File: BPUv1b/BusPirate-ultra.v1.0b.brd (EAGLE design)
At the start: 100 x 50 mm, 176 parts, among them CON1 USB-C-12, IC1 SN74LVC1T45DBV, IC10 23LC1024, IC11 74HCT4051, IC12 MCP1824_ADJ, IC2 SN74LVC1T45DBV, IC3 SN74LVC1T45DBV, IC4 SN74LVC1T45DBV, IC5 SN74LVC1T45DBV, IC6 SN74LVC1T45DBV, IC7 SN74LVC1T45DBV, IC8 SN74LVC1T45DBV, IC9 23LC1024, J1 CON_HEADER_1X04, J2 CON_HEADER_1X10-RIGHT_ANGLED_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, J3 CON_MOLEX_MALE_SMT_SH_1.25, Q1 DMMT3906W, U1 74LVC1G07DBV, U10 74HCT4066PW, U11 74HCT4066PW, U12 W25X40CL, U13 74LVC245A, U14 MCP6001, U15 MCP6001, U16 ICE40HX4K, U2 74LVC1G07DBV, U3 74LVC1G07DBV, U4 74LVC1G07DBV, U5 STM32F103ZX, U6 74LVC1G07DBV, U7 74LVC1G07DBV, U8 74LVC1G07DBV, U9 74LVC1G07DBV

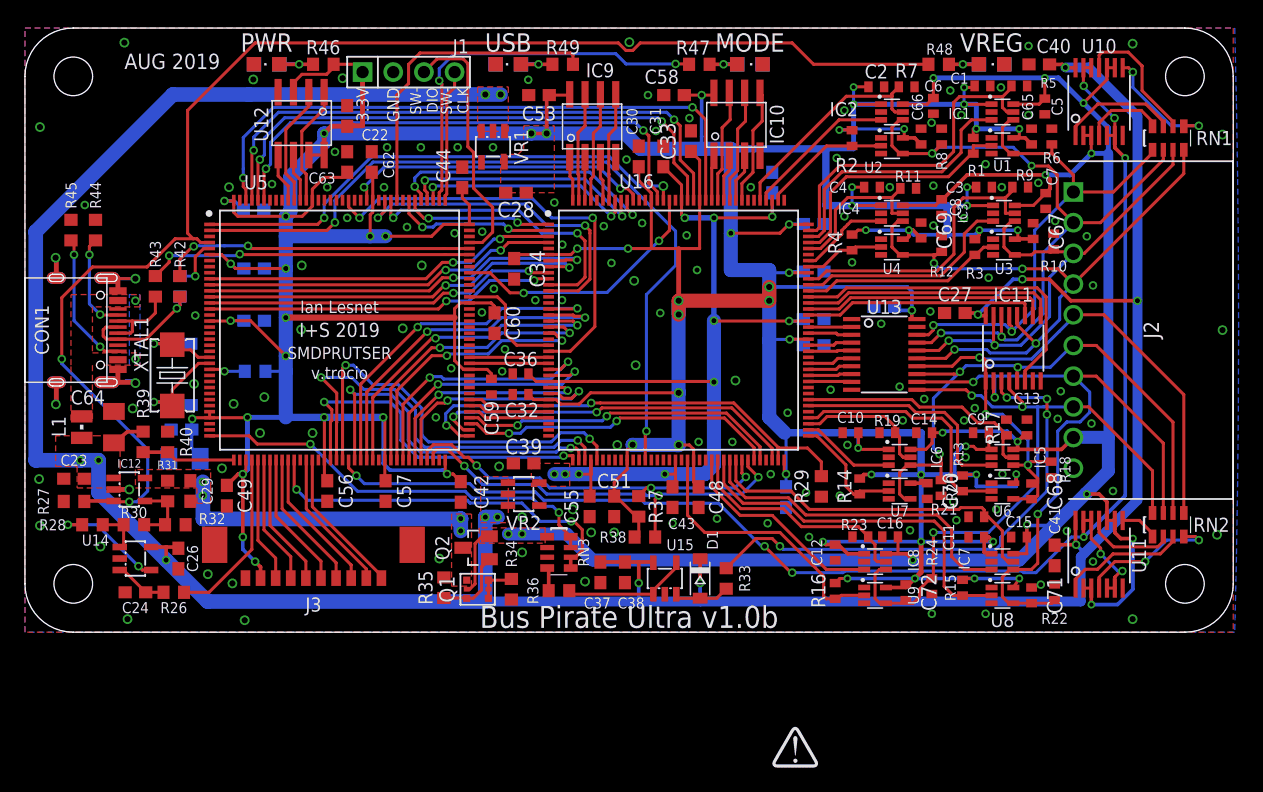
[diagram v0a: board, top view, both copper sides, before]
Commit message: Revert previous commit to v1b, wrong version commited. changes should be on v1c not v1b.
This reverts commit d10a26b079303959180bb4ab2616075854f9b9d1.
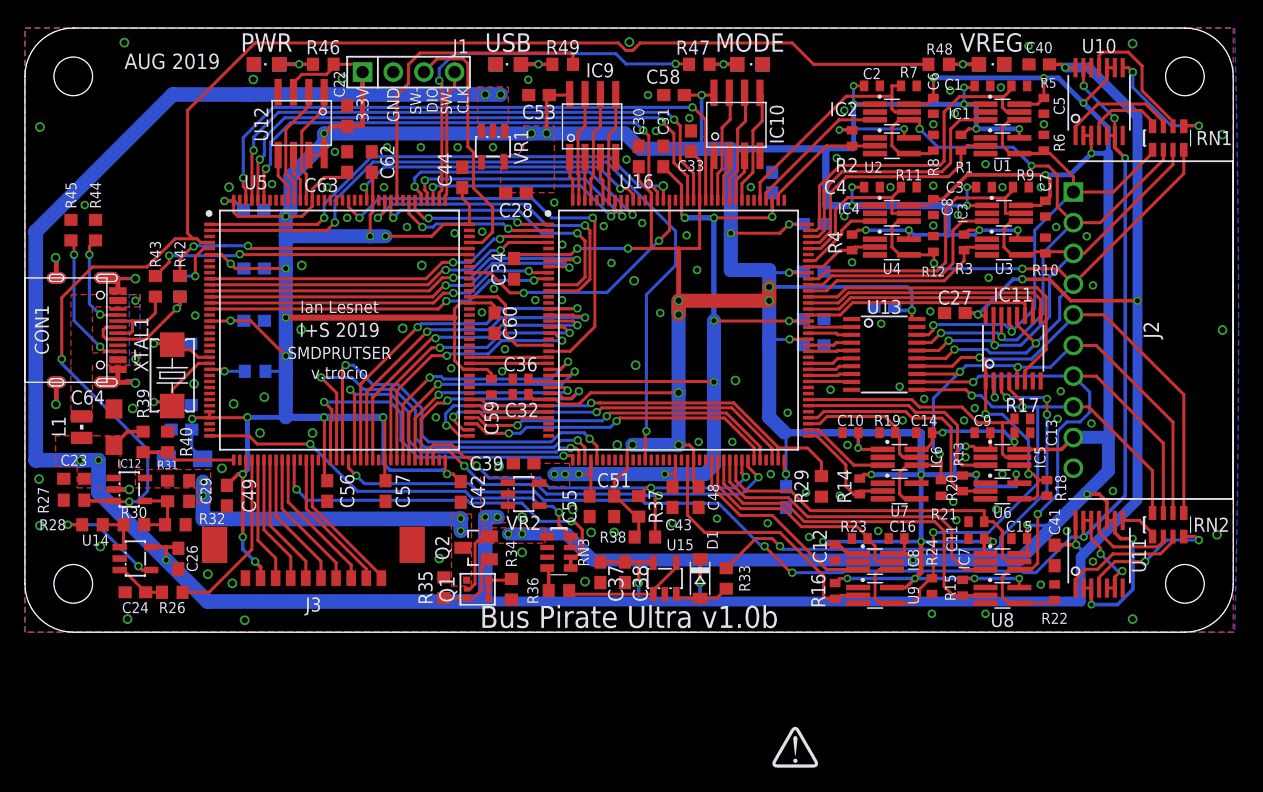
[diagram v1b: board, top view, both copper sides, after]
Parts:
- removed C65, C66, C67, C68, C69, C70, C71, C72: 0.1uF, dp_devices.v6:C402
- C1, C5: device dp_devices.v6:C402 -> rcl:C0402
- C10, C11, C12, C13, C14, C15, C16, C2, C3, C4, C6, C7, C8, C9: device dp_devices.v6:C402 -> resistor:C0402
- C17, C18, C20, C21, C22, C24, C25, C26, C27, C30, C31, C33, C34, C35, C37, C38, C40, C41, C42, C43, C44, C45, C46, C47, C48, C49, C50, C51, C52, C53, C54, C55, C56, C57, C58, C60, C61, C62, C63: device dp_devices.v6:C603 -> rcl:C0603
- C19, C64: device dp_devices.v6:SMC_A -> rcl:SMC_A
- C28, C39: value 1uF -> 1uf; device dp_devices.v6:C603 -> rcl:C0603
- IC1, IC2, IC3, IC4, IC5, IC6, IC7, IC8: device dp_devices.v6:SC-70-6 -> dp_devices.v6:SC-70-6_EXTENDED_PADS
- R1, R10, R11, R12, R13, R14, R15, R16, R17, R18, R19, R2, R20, R21, R22, R23, R24, R3, R4, R5, R6, R7, R8, R9: device dp_devices.v6:R402 -> resistor:R0402
- R26, R29, R37, R38, R41, R42, R43, R44, R45: device dp_devices.v6:R603 -> rcl:R0603
- R33, R36, R39, R40: device dp_devices.v6:R603 -> resistor:R0603
- R46, R47, R48, R49: device dp_devices.v6:R603 -> dp_devices:R603
- U1, U2, U3, U4, U6, U7, U8, U9: device dp_devices.v6:SC-70-5 -> dp_devices.v6:SC-70-5_EXTENDED_PADS
- XTAL1: device dp_devices.v6:XTAL_4X6 -> dp_devices:XTAL_4X6
- moved R18 1.56 mm to (84.6, 11.9)
- moved R17 1.50 mm to (82.5, 17.7), turned to 180 degrees
- moved R1 1.05 mm to (77.5, 40.5)
- moved R3 0.97 mm to (77.7, 32.3)
- moved R8 0.85 mm to (75.2, 40.5)
- moved R6 0.83 mm to (84.3, 40.5)
- moved R10 0.76 mm to (84.5, 32.0)
- moved C8 0.69 mm to (75.2, 35.2), turned to 90 degrees
- moved R12 0.69 mm to (75.2, 32.1)
- moved C7 0.64 mm to (84.5, 35.1), turned to 90 degrees
- moved C13 0.58 mm to (82.5, 16.5), turned to 180 degrees
- moved C16 0.55 mm to (72.1, 7.75), turned to 0 degrees
- moved C36 0.43 mm to (41.0, 21.0)
- moved R21 0.41 mm to (78.7, 9.14)
- moved C2 0.36 mm to (70.1, 45.2), turned to 0 degrees
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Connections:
- net 1V2: now also C31.2, C35.2, C39.1, C43.2, C54.2, C55.2; no longer C31.1, C35.1, C39.2, C43.1, C54.1, C55.1
- net 3V3: now also C1.1, C10.1, C11.1, C12.1, C17.2, C2.1, C21.2, C22.2, C25.2, C28.1, C3.1, C30.2, C33.2, C34.2, C4.1, C42.2, C44.2, C45.2, C46.2, C47.2, C48.2, C49.2, C50.2, C51.2, C52.2, C53.1, C56.2, C57.2, C58.1, C60.2, C61.1, C62.2, C63.2, C9.1; no longer C1.2, C10.2, C11.2, C12.2, C17.1, C2.2, C21.1, C22.1, C25.1, C28.2, C3.2, C30.1, C33.1, C34.1, C4.2, C42.1, C44.1, C45.1, C46.1, C47.1, C48.1, C49.1, C50.1, C51.1, C52.1, C53.2, C56.1, C57.1, C58.2, C60.1, C61.2, C62.1, C63.1, C65.2, C66.2, C67.2, C68.2, C69.2, C70.2, C71.2, C72.2, C9.2
- net GND: now also C1.2, C10.2, C11.2, C12.2, C13.1, C14.1, C15.1, C16.1, C17.1, C18.1, C2.2, C20.1, C21.1, C22.1, C24.2, C25.1, C26.2, C27.2, C28.2, C3.2, C30.1, C31.1, C33.1, C34.1, C35.1, C39.2, C4.2, C40.2, C41.2, C42.1, C43.1, C44.1, C45.1, C46.1, C47.1, C48.1, C49.1, C5.1, C50.1, C51.1, C52.1, C53.2, C54.1, C55.1, C56.1, C57.1, C58.2, C6.1, C60.1, C61.2, C62.1, C63.1, C7.1, C8.1, C9.2; no longer C1.1, C10.1, C11.1, C12.1, C13.2, C14.2, C15.2, C16.2, C17.2, C18.2, C2.1, C20.2, C21.2, C22.2, C24.1, C25.2, C26.1, C27.1, C28.1, C3.1, C30.2, C31.2, C33.2, C34.2, C35.2, C39.1, C4.1, C40.1, C41.1, C42.2, C43.2, C44.2, C45.2, C46.2, C47.2, C48.2, C49.2, C5.2, C50.2, C51.2, C52.2, C53.1, C54.2, C55.2, C56.2, C57.2, C58.1, C6.2, C60.2, C61.1, C62.2, C63.2, C65.1, C66.1, C67.1, C68.1, C69.1, C7.2, C70.1, C71.1, C72.1, C8.2, C9.1
- net N$31: now also C24.1; no longer C24.2
- net N$8: now also C20.2; no longer C20.1
- net N$9: now also C18.2; no longer C18.1
- net VREF/VOUT: now also C13.2, C14.2, C15.2, C16.2, C5.2, C6.2, C7.2, C8.2; no longer C13.1, C14.1, C15.1, C16.1, C5.1, C6.1, C7.1, C8.1
- net VUSB: now also C26.1, C27.1, C40.1, C41.1; no longer C26.2, C27.2, C40.2, C41.2
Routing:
- net 3V3: track 586.3 -> 573.9 mm
- net VREF/VOUT: track 191.3 -> 187.0 mm
- net BPIO1: track 56.1 -> 58.7 mm
- net BUFDIR4: track 20.4 -> 22.1 mm
- net BPIO4: track 56.4 -> 55.2 mm
- net BUFDIR1: track 18.4 -> 19.5 mm
- net BUFDIR2: track 24.9 -> 25.8 mm
- net BUFDIR3: track 13.1 -> 13.7 mm
- net BUFDIR0: track 28.2 -> 28.8 mm
- net BUFDIR6: track 29.2 -> 29.7 mm
- net BPIO2: track 42.7 -> 43.3 mm
- net BUFOD7: track 23.1 -> 22.6 mm
- net BUFOD5: track 9.96 -> 9.46 mm
- net BUFOD4: track 20.7 -> 20.2 mm
- net BUFOD3: track 6.69 -> 6.19 mm
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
